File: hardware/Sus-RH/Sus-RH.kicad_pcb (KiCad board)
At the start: 2 copper layers, 47.8 x 62 mm, 46 parts, among them J1 MX150_02x06_Vertical, J2 53307-2471, J4 Conn_01x06, J5 Conn_01x06, U1 TLV9002QDRQ1, U2 LDO40LPURY

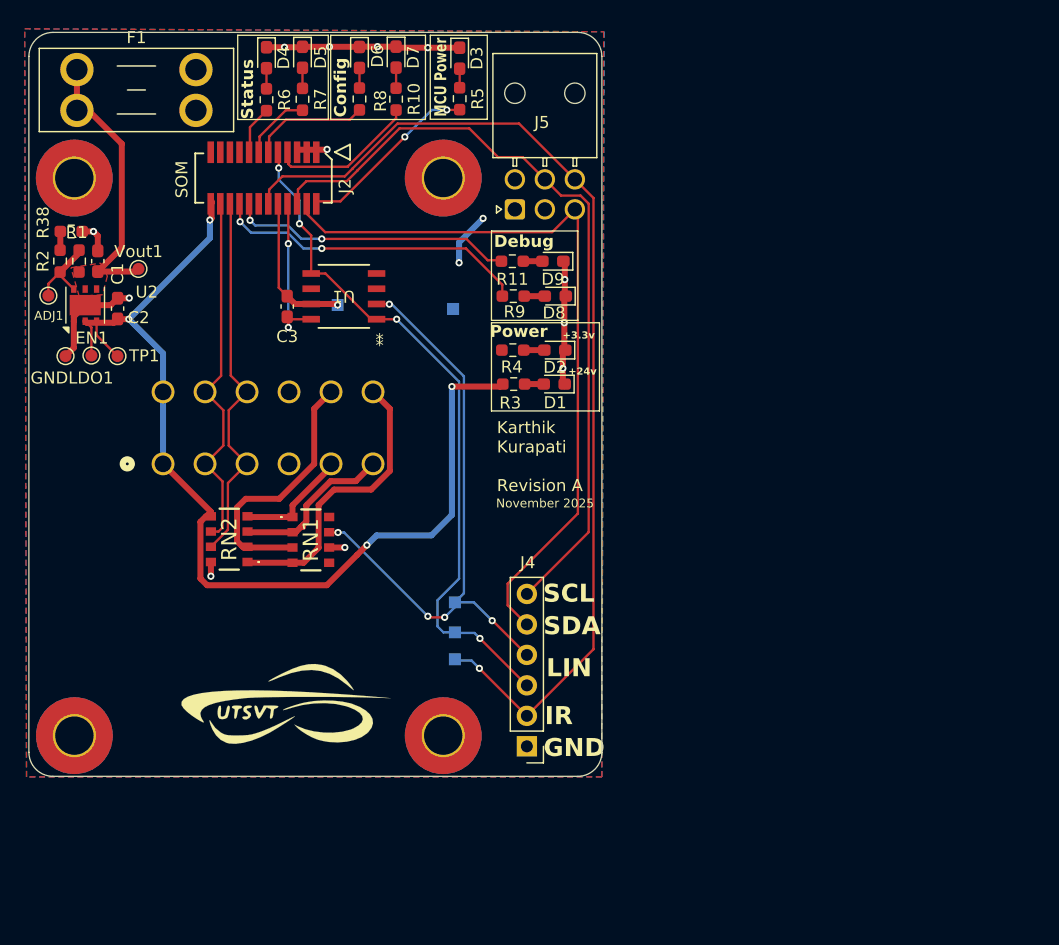
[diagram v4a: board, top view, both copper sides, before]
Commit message: Rev B Review (#2)
* schematic changes: ldo switched out of qfn, op amp footprint fixed, resistor array changed. need add correct stm changes

* finished sch + removed LDO

* removed LDO, added correct cube.

* op-amp changes

* layout finished, need to add some more silkscreen + ready for review!

* finished layout + silkscreen, ready to review.

* mac files removed

* made changes from review council

* added 3d models for 01x05 nanofits

* added stepfiles for sus-rh

* sus-rh production ready

* remove .DS_Store files

* fixed nanofit for linpot

* added "validated silkscreen"

* Added jlc assembly files

* pitot board sch review. the biggest change was the switch to nanofits and different pressure sensor

---------

Co-authored-by: Lakshay983 <56173382+Lakshay983@users.noreply.github.com>
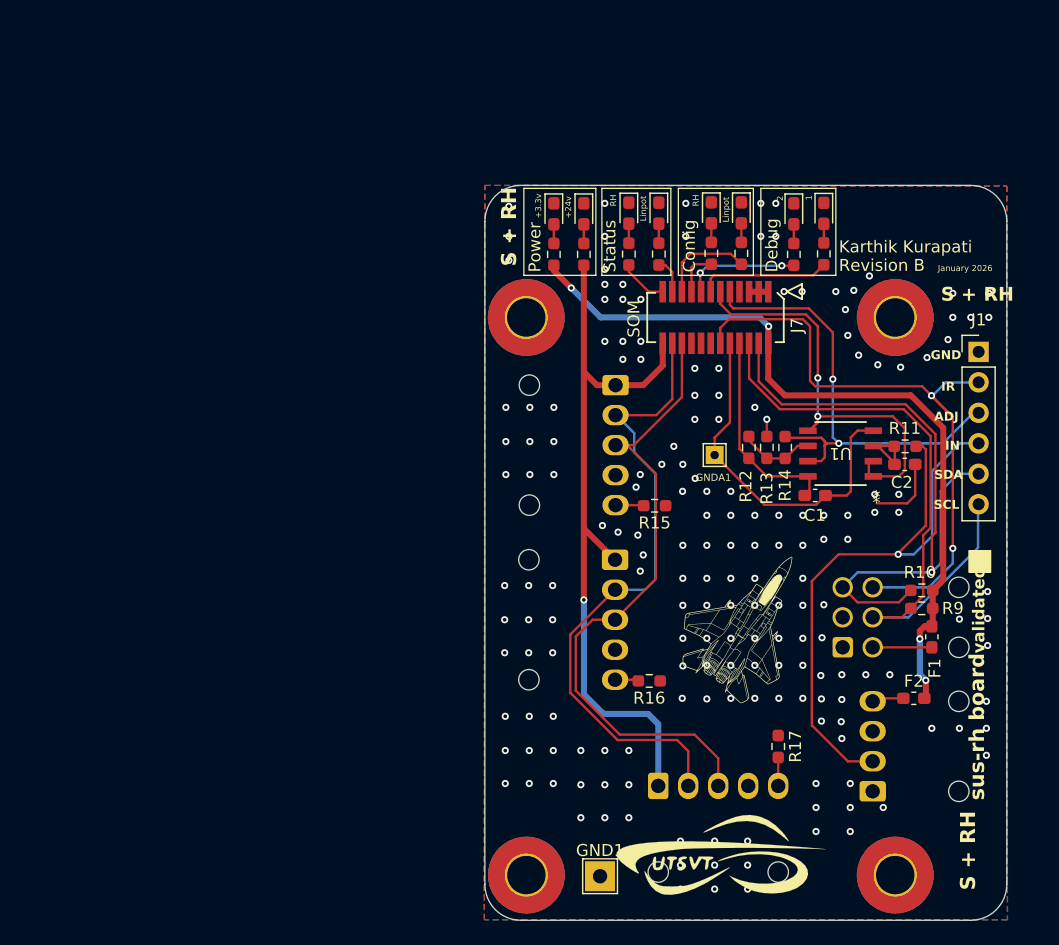
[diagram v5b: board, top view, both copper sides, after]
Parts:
- removed ADJ1, EN1, GNDLDO1: TestPoint, TestPoint:TestPoint_Pad_D1.0mm
- removed C3: 0.1uF, Capacitor_SMD:C_0603_1608Metric_Pad1.08x0.95mm_HandSolder
- removed D9: LED, LED_SMD:LED_0603_1608Metric_Pad1.05x0.95mm_HandSolder
- removed the G*** at (111.4, 66.7)
- removed R38: 2.49k, Resistor_SMD:R_0603_1608Metric_Pad0.98x0.95mm_HandSolder
- removed RN1, RN2: YC324-JK-070RL, 4pinRes:YC324JK07220RL
- removed TP1: Vin, TestPoint:TestPoint_Pad_D1.0mm
- removed U2: LDO40LPURY, Package_DFN_QFN:DFN-6-1EP_3x3mm_P0.95mm_EP1.7x2.6mm
- removed Vout1: TP1, TestPoint:TestPoint_Pad_D1.0mm
- removed ir_interrupt1, linpot_norm1, linpot_out1: TestPoint, TestPoint:TestPoint_Pad_1.0x1.0mm
- added F2: 500mA, Fuse:Fuse_0603_1608Metric_Pad1.05x0.95mm_HandSolder, F.Cu at (140.0, 83.0)
- added G***: LHRs_LOGO, UTSVT_Logos:LHRs_LOGO, F.Cu at (140.8, 43.0)
- added G***: LOGO, custom:plane10, F.Cu at (125.7, 77.4)
- added G***: LOGO, custom:golem_inverted, B.Cu at (135.5, 66.1)
- added G***: LOGO, custom:mountian43.55, B.Cu at (126.1, 90.8)
- added G***: LHRs_LOGO, UTSVT_Logos:LHRs_LOGO, B.Cu at (139.9, 43.0)
- added G***: LOGO, custom:plane10, B.Cu at (125.3, 77.3)
- added J3: Conn_01x05, Connector_Molex:Molex_Nano-Fit_105313-xx05_1x05_P2.50mm_Horizontal, B.Cu at (115.1, 56.9)
- added J6: Conn_01x04, Connector_Molex:Molex_Nano-Fit_105313-xx04_1x04_P2.50mm_Horizontal, B.Cu at (136.6, 90.8)
- added J7: 53307-2471, UTSVT_Connectors:PeripheralSOM, F.Cu at (123.5, 51.3)
- added R12: 4.7k, Resistor_SMD:R_0603_1608Metric_Pad0.98x0.95mm_HandSolder, F.Cu at (126.2, 62.1)
- added R13: 1k, Resistor_SMD:R_0603_1608Metric_Pad0.98x0.95mm_HandSolder, F.Cu at (127.8, 62.1)
- added R14: 0, Resistor_SMD:R_0603_1608Metric_Pad0.98x0.95mm_HandSolder, F.Cu at (129.3, 62.1)
- added R15: 0, Resistor_SMD:R_0603_1608Metric_Pad0.98x0.95mm_HandSolder, F.Cu at (118.4, 67.0)
- added R16: 0, Resistor_SMD:R_0603_1608Metric_Pad0.98x0.95mm_HandSolder, F.Cu at (118.0, 81.5)
- added R17: 0, Resistor_SMD:R_0603_1608Metric_Pad0.98x0.95mm_HandSolder, F.Cu at (128.7, 87.0)
- C1: value 1uF -> 0.1uF
- F1: footprint Fuse:Fuseholder_Blade_Mini_Keystone_3568 -> Fuse:Fuse_0603_1608Metric_Pad1.05x0.95mm_HandSolder
- GND1: footprint TestPoint:TestPoint_Pad_1.0x1.0mm -> TestPoint:TestPoint_THTPad_2.5x2.5mm_Drill1.2mm; moved to F.Cu
- GNDA1: footprint TestPoint:TestPoint_Pad_1.0x1.0mm -> TestPoint:TestPoint_THTPad_1.5x1.5mm_Drill0.7mm; moved to F.Cu
- J1: value MX150_02x06_Vertical -> Conn_01x06; footprint UTSVT_Connectors:MX150_02x06_Vertical -> Connector_PinHeader_2.54mm:PinHeader_1x06_P2.54mm_Vertical; moved to F.Cu
- J2: value 53307-2471 -> Conn_01x05; footprint UTSVT_Connectors:PeripheralSOM -> Connector_Molex:Molex_Nano-Fit_105313-xx05_1x05_P2.50mm_Horizontal; moved to B.Cu
- J4: value Conn_01x06 -> Conn_01x05; footprint Connector_PinHeader_2.54mm:PinHeader_1x06_P2.54mm_Vertical -> Connector_Molex:Molex_Nano-Fit_105313-xx05_1x05_P2.50mm_Horizontal; moved to B.Cu
- J5: moved to B.Cu
- R1: value 10k -> 1k
- R10, R11, R9: value 1k -> 4.7k
- R2: value 15k -> 1k
- R3: value 4.7k -> 1k
- R4, R5, R6, R7: value 120 -> 1k
- U1: footprint footprints:SOIC8_D_TEX -> custom:SOIC8_D_TEX
- moved F1 85.5 mm to (141.5, 77.9), turned to 90 degrees
- moved J1 68.6 mm to (145.4, 54.1)
- moved C2 66.9 mm to (139.2, 63.5), turned to 0 degrees
- moved C1 62.9 mm to (131.8, 66.1), turned to 0 degrees
- moved J2 60.4 mm to (118.7, 90.3), turned to -90 degrees
- moved R10 60.0 mm to (140.7, 74.0), turned to 180 degrees
- moved G*** 58.8 mm to (130.1, 54.1)
- moved R2 56.8 mm to (125.6, 45.9)
- moved R1 52.7 mm to (123.1, 45.9)
- moved GND1 48.8 mm to (113.8, 97.8), turned to 0 degrees
- moved J5 45.6 mm to (134.1, 78.8), turned to 0 degrees
- moved U1 43.4 mm to (133.9, 62.6)
- moved R7 42.9 mm to (130.0, 46.0)
- moved R9 42.8 mm to (140.7, 75.5), turned to 180 degrees
- moved R8 40.8 mm to (132.5, 46.0)
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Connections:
- C1 pad 1: Net-(U2-Vout) -> VDDA
- C1 pad 2: GND -> GNDA
- C2 pad 1: +24V -> Net-(U1A-+)
- F1 pad 1: Net-(U2-Vout) -> Net-(J5-Pin_4)
- J1 pad 1: +24V -> GND
- J1 pad 2: /CAN_+ -> /IR_INTER
- J1 pad 3: /CAN_- -> /linpot_adj
- J1 pad 4: GND -> /linpot_in
- J1 pad 5: /Gen_1 -> /SDA
- J1 pad 6: /Gen_2 -> /SCL
- J2 pad 1: GND -> +24V
- J2 pad 2: +3.3VMCU -> /CAN_+
- J2 pad 3: GND -> /CAN_-
- J2 pad 4: /SDA -> GND
- J2 pad 5: GND -> Net-(J2-Pin_5)
- J4 pad 1: GND -> +24V
- J4 pad 2: /IR_INTER -> /CAN_+
- J4 pad 3: /linpot_norm -> /CAN_-
- J4 pad 4: /linpot_out -> GND
- J4 pad 5: /SDA -> Net-(J4-Pin_5)
- J5 pad 1: unconnected-(J5-Pin_1-Pad1) -> GND
- J5 pad 4: +3.3V -> Net-(J5-Pin_4)
- R1 pad 1: Net-(U2-Vout) -> /RHConfig
- R1 pad 2: Net-(U2-ADJ) -> Net-(D1-A)
- R10 pad 1: /SusConfig -> +3.3V
- R10 pad 2: Net-(D7-A) -> /SDA
- R11 pad 1: /Debug1 -> /linpot_in
- R11 pad 2: Net-(D9-A) -> Net-(U1A-+)
- R2 pad 1: Net-(U2-ADJ) -> /SusConfig
- R2 pad 2: Net-(R2-Pad2) -> Net-(D2-A)
- R3 pad 1: +24V -> /RH_STATUS
- R3 pad 2: Net-(D1-A) -> Net-(D3-A)
- R4 pad 1: +3.3V -> +24V
- R4 pad 2: Net-(D2-A) -> Net-(D4-A)
- R5 pad 1: +3.3VMCU -> /LINPOT_STATUS
- R5 pad 2: Net-(D3-A) -> Net-(D5-A)
- R6 pad 1: /RH_STATUS -> +3.3V
- R6 pad 2: Net-(D4-A) -> Net-(D6-A)
- R7 pad 1: /LINPOT_STATUS -> /Debug2
- R7 pad 2: Net-(D5-A) -> Net-(D7-A)
- R8 pad 1: /RHConfig -> /Debug1
- R8 pad 2: Net-(D6-A) -> Net-(D8-A)
- R9 pad 1: /Debug2 -> +3.3V
- R9 pad 2: Net-(D8-A) -> /SCL
- U1 pad 1: /linpot_norm -> /linpot_out
- U1 pad 3: unconnected-(U1-IN2--Pad3) -> Net-(U1A-+)
- U1 pad 4: unconnected-(U1-IN2+-Pad4) -> GNDA
- U1 pad 5: /linpot_norm -> /linpot_out
- U1 pad 6: unconnected-(U1-OUT2-Pad6) -> Net-(U1B--)
- U1 pad 7: GNDA -> /linpot_adj
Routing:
- net +3.3V: track 4.53 -> 64.9 mm, vias 2 -> 4
- net /linpot_norm: track 58.1 -> 0.00 mm, vias 4 -> 0
- net /linpot_in: track 0.00 -> 50.9 mm, vias 0 -> 1
- net /linpot_adj: track 0.00 -> 41.2 mm, vias 0 -> 2
- net GND: track 43.3 -> 9.05 mm, vias 12 -> 182
- net /IR_INTER: track 86.3 -> 53.6 mm, vias 1 -> 2
- net +24V: track 87.1 -> 61.4 mm, vias 4 -> 1
- net /Gen_4: track 24.3 -> 0.00 mm
- net Net-(U2-Vout): track 23.3 -> 0.00 mm
- net /CAN_-: track 31.9 -> 54.5 mm
- net /Gen_3: track 22.2 -> 0.00 mm
- net /CAN_+: track 31.4 -> 53.6 mm
- net /Debug2: track 26.7 -> 9.65 mm
- net GNDA: track 12.7 -> 29.6 mm, vias 1 -> 0
- net +3.3VMCU: track 15.2 -> 0.00 mm, vias 2 -> 0
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- added copper zone on F.Cu, net GND
- removed copper zone on F.Cu, net +3.3V
- removed copper zone on F.Cu, net Net-(U2-Vout)
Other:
- board size 47.8 x 62 mm -> 43.5 x 61.2 mm
- board text added: "1"
- board text added: "2"
- board text added: "3.3v"
- board text added: "ADJ"
- board text added: "CAN_H"
- board text added: "CAN_L"
- board text added: "GND1"
- board text added: "GNDA1"
- board text added: "IN"
- board text added: "INT"
- board text added: "Input"
- board text added: "January 2026"
- board text added: "Karthik Kurapati"
- board text added: "LINPOT"
- board text added: "Linpot"
- board text added: "OUTPUT"
- board text added: "RH"
- board text added: "RIDEHEIGHT"
- board text added: "Revision B"
- board text added: "S + RH"
- board text added: "SHEILD"
- board text added: "WHEELS"
- board text added: "sus-rh board"
- board text added: "validated"
- board text removed: "Karthik Kurapati Revision A"
- board text removed: "LIN"
- board text removed: "MCU Power"
- board text removed: "November 2025"
